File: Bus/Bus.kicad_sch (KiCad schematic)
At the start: 31 parts, among them J1 Conn_01x22, J2 Conn_01x22, J3 Conn_01x22, J4 Conn_01x22, J5 Conn_01x16, J6 Conn_01x16, J7 Conn_01x16, J8 Conn_01x16, U1 74HC139, U2 SN74HC04N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

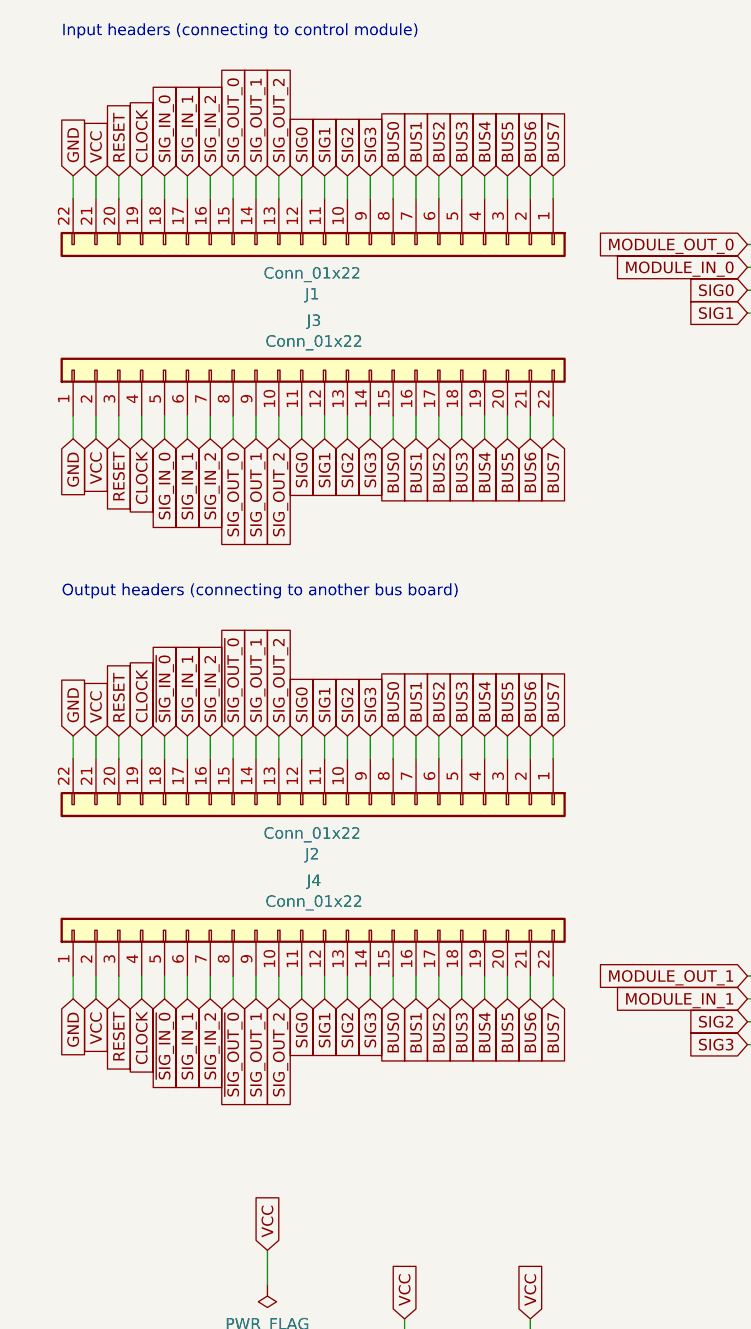
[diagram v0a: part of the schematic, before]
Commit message: Make bus board 4L with ground planes and extra GND connectors
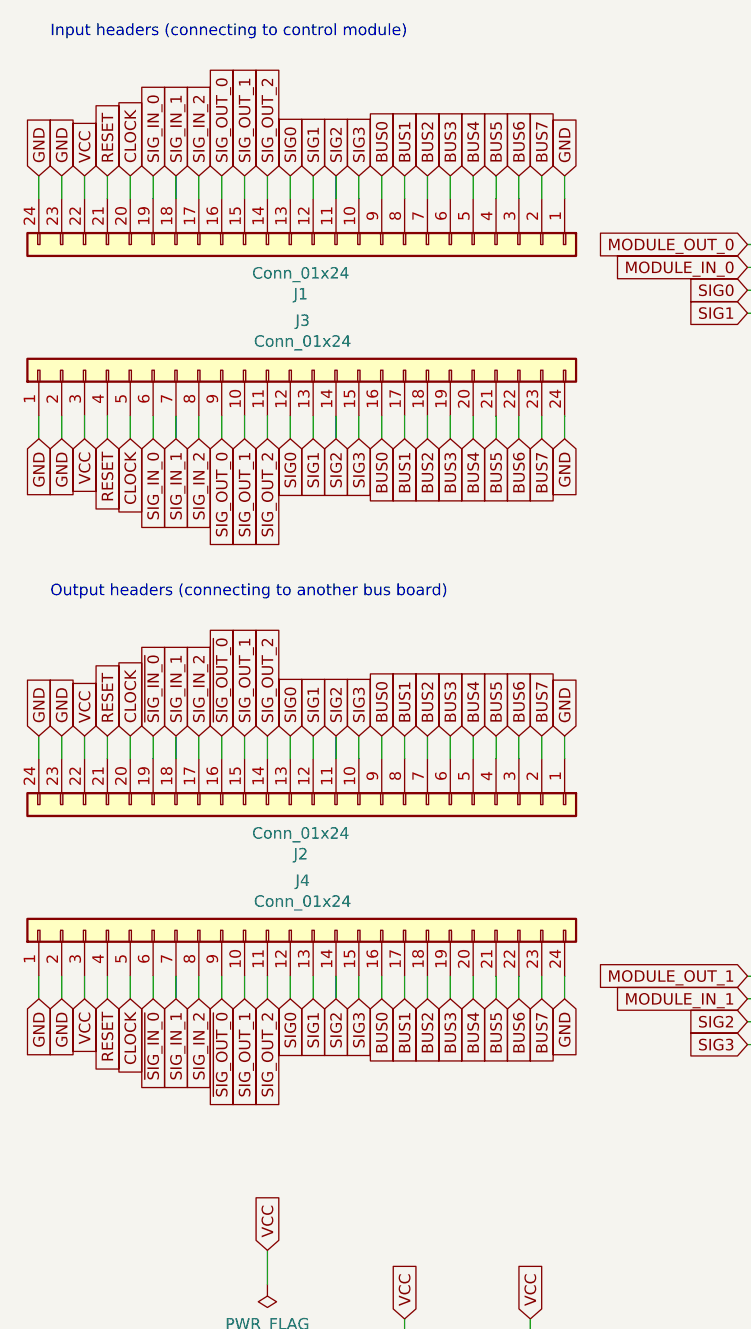
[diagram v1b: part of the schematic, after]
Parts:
- J1, J3: value Conn_01x22 -> Conn_01x24; footprint Connector_PinHeader_2.54mm:PinHeader_1x22_P2.54mm_Horizontal -> Connector_PinHeader_2.54mm:PinHeader_1x24_P2.54mm_Horizontal; symbol Connector_Generic:Conn_01x22 -> Connector_Generic:Conn_01x24
- J2, J4: value Conn_01x22 -> Conn_01x24; footprint Connector_PinSocket_2.54mm:PinSocket_1x22_P2.54mm_Horizontal -> Connector_PinSocket_2.54mm:PinSocket_1x24_P2.54mm_Horizontal; symbol Connector_Generic:Conn_01x22 -> Connector_Generic:Conn_01x24
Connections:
- net BUS0: now also J1.9 (Pin_9), J2.9 (Pin_9), J3.16 (Pin_16), J4.16 (Pin_16); no longer J1.8 (Pin_8), J2.8 (Pin_8), J3.15 (Pin_15), J4.15 (Pin_15)
- net BUS1: now also J1.8 (Pin_8), J2.8 (Pin_8), J3.17 (Pin_17), J4.17 (Pin_17); no longer J1.7 (Pin_7), J2.7 (Pin_7), J3.16 (Pin_16), J4.16 (Pin_16)
- net BUS2: now also J1.7 (Pin_7), J2.7 (Pin_7), J3.18 (Pin_18), J4.18 (Pin_18); no longer J1.6 (Pin_6), J2.6 (Pin_6), J3.17 (Pin_17), J4.17 (Pin_17)
- net BUS3: now also J1.6 (Pin_6), J2.6 (Pin_6), J3.19 (Pin_19), J4.19 (Pin_19); no longer J1.5 (Pin_5), J2.5 (Pin_5), J3.18 (Pin_18), J4.18 (Pin_18)
- net BUS4: now also J1.5 (Pin_5), J2.5 (Pin_5), J3.20 (Pin_20), J4.20 (Pin_20); no longer J1.4 (Pin_4), J2.4 (Pin_4), J3.19 (Pin_19), J4.19 (Pin_19)
- net BUS5: now also J1.4 (Pin_4), J2.4 (Pin_4), J3.21 (Pin_21), J4.21 (Pin_21); no longer J1.3 (Pin_3), J2.3 (Pin_3), J3.20 (Pin_20), J4.20 (Pin_20)
- net BUS6: now also J1.3 (Pin_3), J2.3 (Pin_3), J3.22 (Pin_22), J4.22 (Pin_22); no longer J1.2 (Pin_2), J2.2 (Pin_2), J3.21 (Pin_21), J4.21 (Pin_21)
- net BUS7: now also J1.2 (Pin_2), J2.2 (Pin_2), J3.23 (Pin_23), J4.23 (Pin_23); no longer J1.1 (Pin_1), J2.1 (Pin_1), J3.22 (Pin_22), J4.22 (Pin_22)
- net CLOCK: now also J1.20 (Pin_20), J2.20 (Pin_20), J3.5 (Pin_5), J4.5 (Pin_5); no longer J1.19 (Pin_19), J2.19 (Pin_19), J3.4 (Pin_4), J4.4 (Pin_4)
- net GND: now also J1.1 (Pin_1), J1.23 (Pin_23), J1.24 (Pin_24), J2.1 (Pin_1), J2.23 (Pin_23), J2.24 (Pin_24), J3.2 (Pin_2), J3.24 (Pin_24), J4.2 (Pin_2), J4.24 (Pin_24); no longer J1.22 (Pin_22), J2.22 (Pin_22)
- net RESET: now also J1.21 (Pin_21), J2.21 (Pin_21), J3.4 (Pin_4), J4.4 (Pin_4); no longer J1.20 (Pin_20), J2.20 (Pin_20), J3.3 (Pin_3), J4.3 (Pin_3)
- net SIG0: now also J1.13 (Pin_13), J2.13 (Pin_13), J3.12 (Pin_12), J4.12 (Pin_12); no longer J1.12 (Pin_12), J2.12 (Pin_12), J3.11 (Pin_11), J4.11 (Pin_11)
- net SIG1: now also J1.12 (Pin_12), J2.12 (Pin_12), J3.13 (Pin_13), J4.13 (Pin_13); no longer J1.11 (Pin_11), J2.11 (Pin_11), J3.12 (Pin_12), J4.12 (Pin_12)
- net SIG2: now also J1.11 (Pin_11), J2.11 (Pin_11), J3.14 (Pin_14), J4.14 (Pin_14); no longer J1.10 (Pin_10), J2.10 (Pin_10), J3.13 (Pin_13), J4.13 (Pin_13)
- net SIG3: now also J1.10 (Pin_10), J2.10 (Pin_10), J3.15 (Pin_15), J4.15 (Pin_15); no longer J1.9 (Pin_9), J2.9 (Pin_9), J3.14 (Pin_14), J4.14 (Pin_14)
- net SIG_IN_0: now also J1.19 (Pin_19), J3.6 (Pin_6); no longer J1.18 (Pin_18), J3.5 (Pin_5)
- net SIG_IN_1: now also J1.18 (Pin_18), J2.18 (Pin_18), J3.7 (Pin_7), J4.7 (Pin_7); no longer J1.17 (Pin_17), J2.17 (Pin_17), J3.6 (Pin_6), J4.6 (Pin_6)
- net SIG_IN_2: now also J1.17 (Pin_17), J2.17 (Pin_17), J3.8 (Pin_8), J4.8 (Pin_8); no longer J1.16 (Pin_16), J2.16 (Pin_16), J3.7 (Pin_7), J4.7 (Pin_7)
- net SIG_OUT_0: now also J1.16 (Pin_16), J3.9 (Pin_9); no longer J1.15 (Pin_15), J3.8 (Pin_8)
- net SIG_OUT_1: now also J1.15 (Pin_15), J2.15 (Pin_15), J3.10 (Pin_10), J4.10 (Pin_10); no longer J1.14 (Pin_14), J2.14 (Pin_14), J3.9 (Pin_9), J4.9 (Pin_9)
- net SIG_OUT_2: now also J1.14 (Pin_14), J2.14 (Pin_14), J3.11 (Pin_11), J4.11 (Pin_11); no longer J1.13 (Pin_13), J2.13 (Pin_13), J3.10 (Pin_10), J4.10 (Pin_10)
- net VCC: now also J1.22 (Pin_22), J2.22 (Pin_22), J3.3 (Pin_3), J4.3 (Pin_3); no longer J1.21 (Pin_21), J2.21 (Pin_21), J3.2 (Pin_2), J4.2 (Pin_2)
- net ~{SIG_IN_0}: now also J2.19 (Pin_19), J4.6 (Pin_6); no longer J2.18 (Pin_18), J4.5 (Pin_5)
- net ~{SIG_OUT_0}: now also J2.16 (Pin_16), J4.9 (Pin_9); no longer J2.15 (Pin_15), J4.8 (Pin_8)
